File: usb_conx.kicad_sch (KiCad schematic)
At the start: 9 parts, among them J57 USB_B_Micro, J58 Conn_01x04, U30 TS3USB3000RSE, U31 AP22653AW6-7

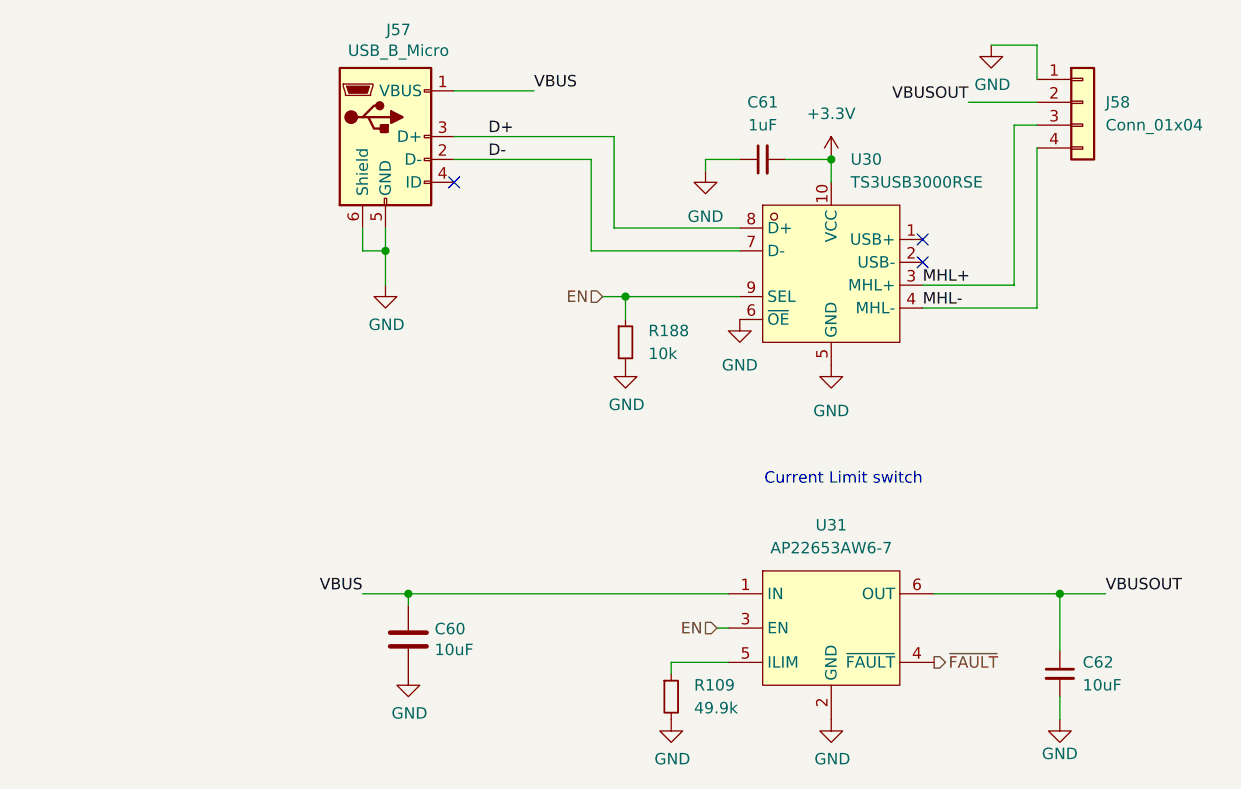
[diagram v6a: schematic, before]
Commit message: Improve MCU2 layout; document curlim12v CSA
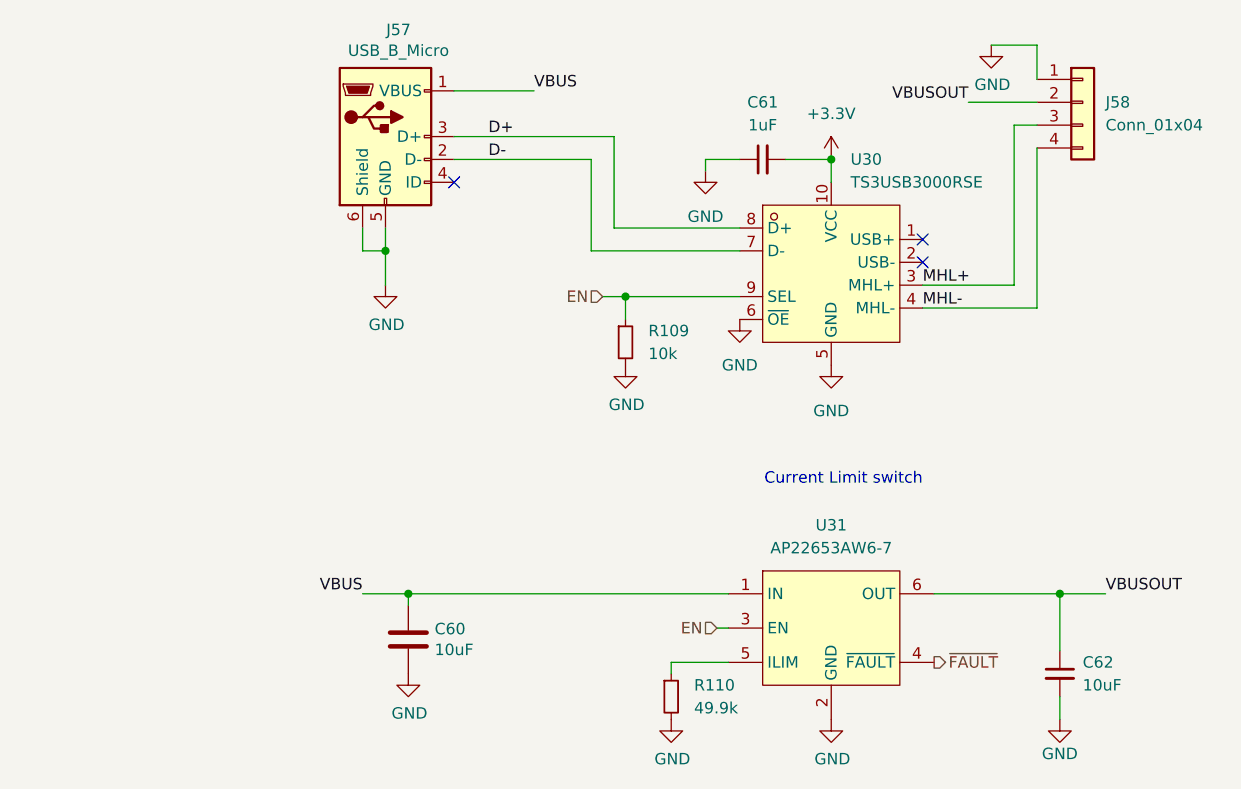
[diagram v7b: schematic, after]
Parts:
- renumbered R188 to R109, R109 to R110
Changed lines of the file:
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@@
+		(polyline
+			(pts
+				(xy 127 73.66) (xy 129.54 73.66) (xy 129.54 80.01) (xy 127 80.01)
+			)
+			(stroke
+				(width 0)
+				(type dash)
+			)
+			(fill
+				(type none)
+			)
+		)
+	)
+	(rule_area
 		(polyline
 			(pts
 				(xy 179.07 90.17) (xy 176.53 90.17) (xy 176.53 96.52) (xy 179.07 96.52)
-			)
-			(stroke
-				(width 0)
-				(type dash)
-			)
-			(fill
-				(type none)
-			)
-		)
-	)
-	(rule_area
-		(polyline
-			(pts
-				(xy 127 73.66) (xy 129.54 73.66) (xy 129.54 80.01) (xy 127 80.01)
 			)
 			(stroke
@@
 		(on_board yes)
 		(dnp no)
-		(property "Reference" "#PWR0233"
+		(property "Reference" "#PWR0234"
 			(at 160.02 146.05 0)
 			(effects
@@
 			(project "HALSPA"
 				(path "/7eeba806-440e-4671-bc07-69fe183910a7/e58e5285-b72c-4e4c-88bb-30be4b81421e"
-					(reference "#PWR0233")
+					(reference "#PWR0234")
 					(unit 1)
 				)
@@
 		(on_board yes)
 		(dnp no)
-		(property "Reference" "#PWR0228"
+		(property "Reference" "#PWR0229"
 			(at 142.24 146.05 0)
 			(effects
@@
 			(project "HALSPA"
 				(path "/7eeba806-440e-4671-bc07-69fe183910a7/e58e5285-b72c-4e4c-88bb-30be4b81421e"
-					(reference "#PWR0228")
+					(reference "#PWR0229")
 					(unit 1)
 				)
@@
 		(dnp no)
 		(fields_autoplaced yes)
-		(property "Reference" "#PWR0232"
+		(property "Reference" "#PWR0233"
 			(at 160.02 106.68 0)
 			(effects
@@
 			(project "HALSPA"
 				(path "/7eeba806-440e-4671-bc07-69fe183910a7/e58e5285-b72c-4e4c-88bb-30be4b81421e"
-					(reference "#PWR0232")
+					(reference "#PWR0233")
 					(unit 1)
 				)
@@
 		(dnp no)
 		(fields_autoplaced yes)
-		(property "Reference" "#PWR0230"
+		(property "Reference" "#PWR0231"
 			(at 149.86 101.6 0)
 			(effects
@@
 			(project ""
 				(path "/7eeba806-440e-4671-bc07-69fe183910a7/e58e5285-b72c-4e4c-88bb-30be4b81421e"
-					(reference "#PWR0230")
+					(reference "#PWR0231")
 					(unit 1)
 				)
@@
 		(dnp no)
 		(fields_autoplaced yes)
-		(property "Reference" "#PWR0231"
+		(property "Reference" "#PWR0232"
 			(at 160.02 81.28 0)
 			(effects
@@
 			(project ""
 				(path "/7eeba806-440e-4671-bc07-69fe183910a7/e58e5285-b72c-4e4c-88bb-30be4b81421e"
-					(reference "#PWR0231")
+					(reference "#PWR0232")
 					(unit 1)
 				)
@@
 		(on_board yes)
 		(dnp no)
-		(property "Reference" "#PWR0272"
+		(property "Reference" "#PWR0228"
 			(at 137.16 106.68 0)
 			(effects
@@
 			(project "HALSPA"
 				(path "/7eeba806-440e-4671-bc07-69fe183910a7/e58e5285-b72c-4e4c-88bb-30be4b81421e"
-					(reference "#PWR0272")
+					(reference "#PWR0228")
 					(unit 1)
 				)
@@
 		(dnp no)
 		(fields_autoplaced yes)
-		(property "Reference" "R188"
+		(property "Reference" "R109"
 			(at 139.7 96.5199 0)
 			(effects
@@
 			(project "HALSPA"
 				(path "/7eeba806-440e-4671-bc07-69fe183910a7/e58e5285-b72c-4e4c-88bb-30be4b81421e"
-					(reference "R188")
+					(reference "R109")
 					(unit 1)
 				)
@@
 		(on_board yes)
 		(dnp no)
-		(property "Reference" "#PWR0235"
+		(property "Reference" "#PWR0236"
 			(at 185.42 146.05 0)
 			(effects
@@
 			(project "HALSPA"
 				(path "/7eeba806-440e-4671-bc07-69fe183910a7/e58e5285-b72c-4e4c-88bb-30be4b81421e"
-					(reference "#PWR0235")
+					(reference "#PWR0236")
 					(unit 1)
 				)
@@
 		(dnp no)
 		(fields_autoplaced yes)
-		(property "Reference" "#PWR0229"
+		(property "Reference" "#PWR0230"
 			(at 146.05 85.09 0)
 			(effects
@@
 			(project "HALSPA"
 				(path "/7eeba806-440e-4671-bc07-69fe183910a7/e58e5285-b72c-4e4c-88bb-30be4b81421e"
-					(reference "#PWR0229")
+					(reference "#PWR0230")
 					(unit 1)
 				)
@@
 		(on_board yes)
 		(dnp no)
-		(property "Reference" "#PWR0234"
+		(property "Reference" "#PWR0235"
 			(at 177.8 71.12 0)
 			(effects
@@
 			(project "HALSPA"
 				(path "/7eeba806-440e-4671-bc07-69fe183910a7/e58e5285-b72c-4e4c-88bb-30be4b81421e"
-					(reference "#PWR0234")
+					(reference "#PWR0235")
 					(unit 1)
 				)
@@
 		(dnp no)
 		(fields_autoplaced yes)
-		(property "Reference" "R109"
+		(property "Reference" "R110"
 			(at 144.78 135.8899 0)
 			(effects
@@
 			(project ""
 				(path "/7eeba806-440e-4671-bc07-69fe183910a7/e58e5285-b72c-4e4c-88bb-30be4b81421e"
-					(reference "R109")
-					(unit 1)
-				)
+					(reference "R110")
+					(unit 1)
+				)
